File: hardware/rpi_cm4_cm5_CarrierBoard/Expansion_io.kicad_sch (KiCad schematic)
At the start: 7 parts, among them J18 0878325922

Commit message: Added power input protection & filter Added dedicated QWIIC connector on RPI CMx I2C6 bus Adjusted power table and PinMux Updated schematics accordingly
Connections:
- net SYS_~{RST} renamed EXP_IO_~{RST}
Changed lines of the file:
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@@
 		)
 	)
-	(hierarchical_label "SYS_~{RST}"
+	(hierarchical_label "EXP_IO_~{RST}"
 		(shape input)
 		(at 83.185 97.155 180)

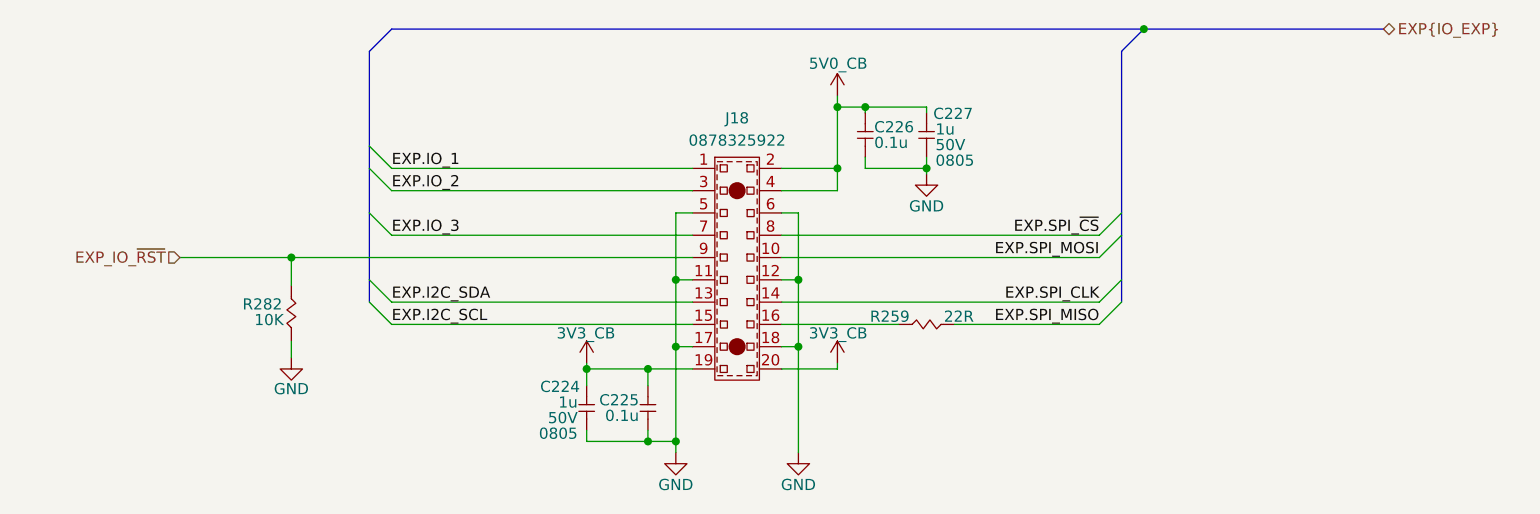
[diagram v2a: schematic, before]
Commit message: Update preliminary placement, update DNP, regen BOM + Preliminary schematics
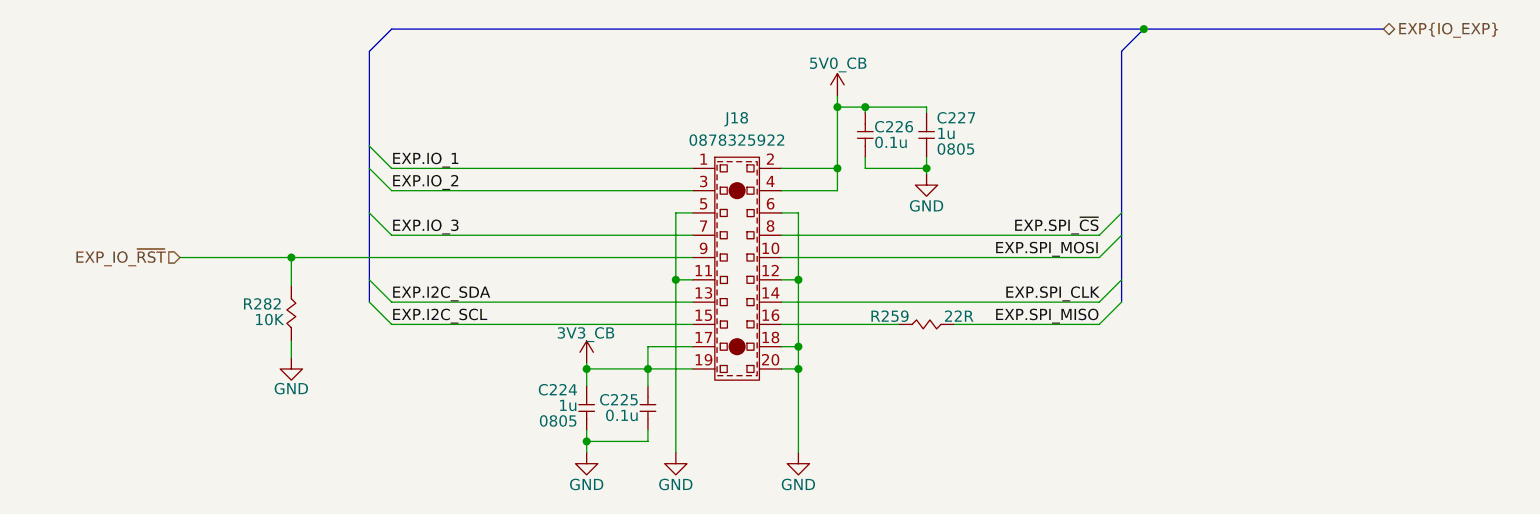
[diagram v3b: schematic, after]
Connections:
- net 3V3_CB: now also J18.17; no longer J18.20
- net GND: now also J18.20; no longer J18.17

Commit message: Update PCB design rules for outer layers differential pairs Update preliminary component placement Update schematics based on PCB placement & remove duplicata / unnecessary components Update design notes and power table
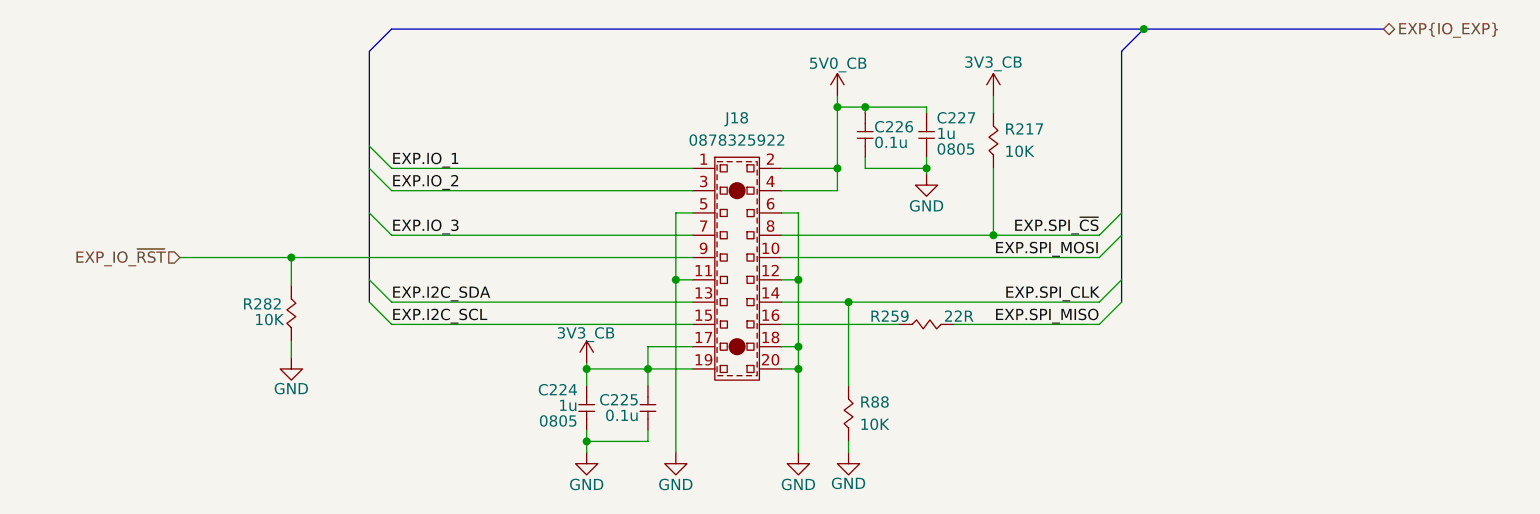
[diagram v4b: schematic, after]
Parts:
- added R217, R88: 10K, footprint:RES_0402, symbol KicadCompDb:Resistors/RES_SMT_00013
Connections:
- net 3V3_CB: now also R217.2
- net EXP.SPI_CLK: now also R88.2
- net EXP.SPI_~{CS}: now also R217.1
- net GND: now also R88.1
